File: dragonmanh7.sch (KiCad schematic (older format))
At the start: 109 parts, among them J1 USB_B, J10 Conn_02x12_Odd_Even, J11 Conn_02x03_Odd_Even, J12 VBAT+, J13 Conn_02x05_Odd_Even, J14 VBATG, J15 Conn_02x02_Odd_Even, J18 Conn_02x05_Odd_Even, J2 USB_A, J3 RJ45_Amphenol_RJMG1BD3B8K1ANR, J4 Micro_SD_Card, J5 Screw_Terminal_01x06, J6 Conn_02x12_Odd_Even, J7 USB_B, J8 Screw_Terminal_01x02, J9 Conn_02x12_Odd_Even, SW1 RESET, SW2 PC13, U1 STM32H743VITx, U10 USBLC6-2SC6, U11 SN6505, U12 TCAN332, U13 ISL83483, U14 MIC2005A, U2 KSZ8081RNA, U3 ISO1050DUB, U4 ISO3082DW, U5 S25FL127SABMFI101, U6 AP63203, U7 USBLC6-2SC6, U8 STM32F042F6Px, U9 USBLC6-2SC6, Y1 8MHz, Y2 32.768KHz, Y3 25MHz

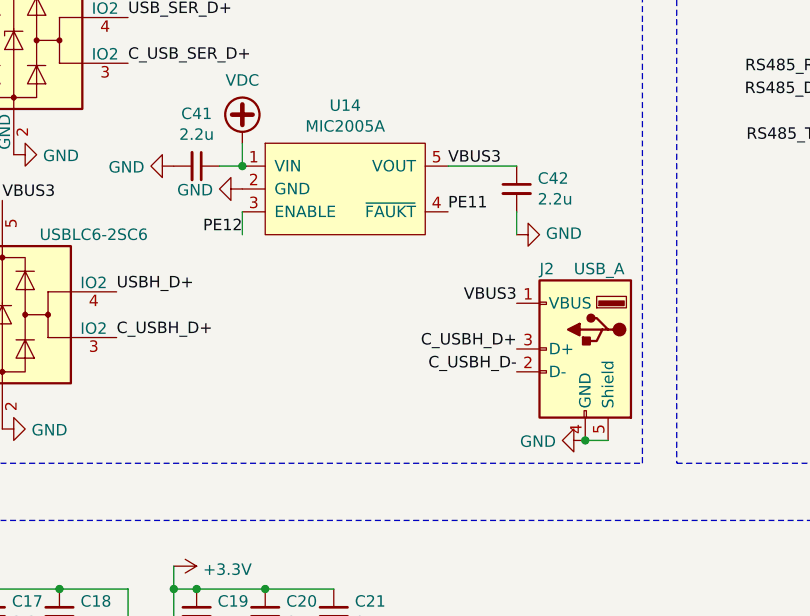
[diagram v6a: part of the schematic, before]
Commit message: Change USB connectors to more hardness versions:
 - OTG1 to USB-B
 - DAP to USB-B
 - OTG2 to USB-A horizontal rigth angle
 - Move leds and buttons to bottom side
 - Align up and bottom headers
 - Add HOST power control on OTG2

Signed-off-by: Martin Ribelotta <martinribelotta@gmail.com>
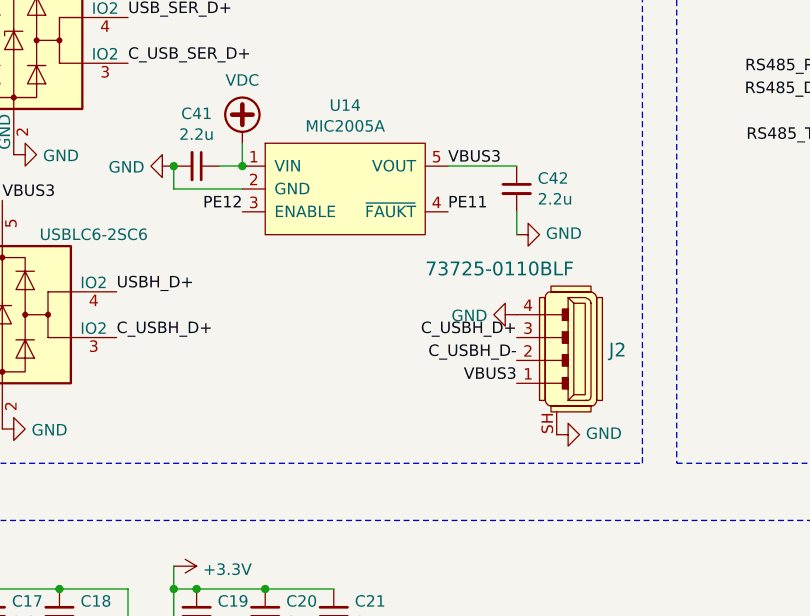
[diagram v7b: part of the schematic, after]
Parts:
- removed J2: USB_A, footprints:USB_A_Female_Vertical_RA_73725-0110BLF, symbol Connector:USB_A
- added J2: 73725-0110BLF, footprints:USB_A_Female_Vertical_RA_73725-0110BLF, symbol dk_USB-DVI-HDMI-Connectors:73725-0110BLF
- J1, J7: manf# (none) -> USB-B-S-RA-WT-SPCC
- U14: manf# (none) -> MIC2005A-2YM5-TR
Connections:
- net C_USBH_D+: now also J2.3
- net C_USBH_D-: now also J2.2
- net GND: now also J2.4, J2.SH
- net VBUS3: now also J2.1
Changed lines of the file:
@@
 C_USBD_D+
 $Comp
-L power:GND #PWR0113
-U 1 1 5C5D013E
-P 8700 7250
-F 0 "#PWR0113" H 8700 7000 50  0001 C CNN
-F 1 "GND" V 8705 7122 50  0000 R CNN
-F 2 "" H 8700 7250 50  0001 C CNN
-F 3 "" H 8700 7250 50  0001 C CNN
-	1    8700 7250
-	0    1    1    0
-$EndComp
-$Comp
 L power:GND #PWR0114
 U 1 1 5C5D01D3
@@
 	0    -1   -1   0
 $EndComp
-Text Label 10700 4200 0    50   ~ 0
-CAN_H
-Text Label 10700 4400 0    50   ~ 0
-CAN_L
-$Comp
-L power:GND #PWR0174
-U 1 1 5C7EED00
-P 10200 4700
-F 0 "#PWR0174" H 10200 4450 50  0001 C CNN
-F 1 "GND" V 10205 4572 50  0000 R CNN
-F 2 "" H 10200 4700 50  0001 C CNN
-F 3 "" H 10200 4700 50  0001 C CNN
-	1    10200 4700
-	0    -1   -1   0
-$EndComp
-Text Label 9700 4200 2    50   ~ 0
-CAN_RX
-Text Label 9700 4100 2    50   ~ 0
-CAN_TX
 $Comp
 L MCU_ST_STM32F0:STM32F042F4Px U8
@@
 Wire Wire Line
 	12050 8600 12150 8600
-Text Label 8400 6850 2    50   ~ 0
+Text Label 8400 6800 2    50   ~ 0
 C_USBH_D+
-Text Label 8400 6950 2    50   ~ 0
+Text Label 8400 6900 2    50   ~ 0
 C_USBH_D-
 $Comp
@@
 F 2 "Connector_USB:USB_B_OST_USB-B1HSxx_Horizontal" H 8850 3750 50  0001 C CNN
 F 3 " ~" H 8850 3750 50  0001 C CNN
+F 4 "USB-B-S-RA-WT-SPCC" H 8700 3800 50  0001 C CNN "manf#"
 	1    8700 3800
 	-1   0    0    -1
@@
 F 2 "Connector_USB:USB_B_OST_USB-B1HSxx_Horizontal" H 8850 4650 50  0001 C CNN
 F 3 " ~" H 8850 4650 50  0001 C CNN
+F 4 "USB-B-S-RA-WT-SPCC" H 8700 4700 50  0001 C CNN "manf#"
 	1    8700 4700
 	-1   0    0    -1
@@
 	8700 5100 8800 5100
 Connection ~ 8700 5100
-$Comp
-L Connector:USB_A J2
-U 1 1 5D52EE8F
-P 8700 6850
-F 0 "J2" H 8900 7200 50  0000 R CNN
-F 1 "USB_A" H 8750 7200 50  0000 R CNN
-F 2 "footprints:USB_A_Female_Vertical_RA_73725-0110BLF" H 8850 6800 50  0001 C CNN
-F 3 " ~" H 8850 6800 50  0001 C CNN
-	1    8700 6850
-	-1   0    0    -1
-$EndComp
-Wire Wire Line
-	8700 7250 8800 7250
-Connection ~ 8700 7250
 Wire Wire Line
 	12050 8200 12050 8600
@@
 F 2 "Package_TO_SOT_SMD:SOT-23-5" H 7650 6150 50  0001 C CNN
 F 3 "" H 7650 6150 50  0001 C CNN
+F 4 "MIC2005A-2YM5-TR" H 7650 6150 50  0001 C CNN "manf#"
 	1    7650 6150
 	1    0    0    -1
@@
 Text Label 6150 6200 0    50   ~ 0
 VBUS3
-Text Label 8400 6650 2    50   ~ 0
+Text Label 8400 7000 2    50   ~ 0
 VBUS3
 Text Label 8100 6050 0    50   ~ 0
 VBUS3
-$Comp
-L power:GND #PWR012
-U 1 1 5D4563D0
-P 7200 6150
-F 0 "#PWR012" H 7200 5900 50  0001 C CNN
-F 1 "GND" V 7205 6022 50  0000 R CNN
-F 2 "" H 7200 6150 50  0001 C CNN
-F 3 "" H 7200 6150 50  0001 C CNN
-	1    7200 6150
-	0    1    1    0
-$EndComp
 Text Label 8100 6250 0    50   ~ 0
 PE11
-Text Label 7200 6350 2    50   ~ 0
+Text Label 7200 6250 2    50   ~ 0
 PE12
-Wire Wire Line
-	7200 6350 7200 6250
 $Comp
 L Device:C_Small C42
@@
 	0    1    1    0
 $EndComp
+Text Label 9700 4100 2    50   ~ 0
+CAN_TX
+Text Label 9700 4200 2    50   ~ 0
+CAN_RX
+Text Label 10700 4200 0    50   ~ 0
+CAN_H
+Text Label 10700 4400 0    50   ~ 0
+CAN_L
+$Comp
+L power:GND #PWR0174
+U 1 1 5C7EED00
+P 10200 4700
+F 0 "#PWR0174" H 10200 4450 50  0001 C CNN
+F 1 "GND" V 10205 4572 50  0000 R CNN
+F 2 "" H 10200 4700 50  0001 C CNN
+F 3 "" H 10200 4700 50  0001 C CNN
+	1    10200 4700
+	0    -1   -1   0
+$EndComp
 $Comp
 L Interface_CAN_LIN:TCAN332 U12
@@
 	1    0    0    -1
 $EndComp
+$Comp
+L dk_USB-DVI-HDMI-Connectors:73725-0110BLF J2
+U 1 1 5D19B1BA
+P 8700 6900
+F 0 "J2" H 8597 6945 60  0000 R CNN
+F 1 "73725-0110BLF" H 9400 7300 60  0000 R CNN
+F 2 "footprints:USB_A_Female_Vertical_RA_73725-0110BLF" H 8900 7100 60  0001 L CNN
+F 3 "" H 8900 7200 60  0001 L CNN
+F 4 "609-1041-ND" H 8900 7300 60  0001 L CNN "Digi-Key_PN"
+F 5 "73725-0110BLF" H 8900 7400 60  0001 L CNN "MPN"
+F 6 "Connectors, Interconnects" H 8900 7500 60  0001 L CNN "Category"
+F 7 "USB, DVI, HDMI Connectors" H 8900 7600 60  0001 L CNN "Family"
+F 8 "http://www.amphenol-icc.com/media/wysiwyg/files/drawing/73725.pdf" H 8900 7700 60  0001 L CNN "DK_Datasheet_Link"
+F 9 "/product-detail/en/amphenol-icc-fci/73725-0110BLF/609-1041-ND/1001355" H 8900 7800 60  0001 L CNN "DK_Detail_Page"
+F 10 "CONN RCPT USB2.0 TYPEA 4POS R/A" H 8900 7900 60  0001 L CNN "Description"
+F 11 "Amphenol ICC (FCI)" H 8900 8000 60  0001 L CNN "Manufacturer"
+F 12 "Active" H 8900 8100 60  0001 L CNN "Status"
+F 13 "73725-0110BLF" H 8700 6900 50  0001 C CNN "manf#"
+	1    8700 6900
+	-1   0    0    -1
+$EndComp
+$Comp
+L power:GND #PWR0113
+U 1 1 5C5D013E
+P 8400 6700
+F 0 "#PWR0113" H 8400 6450 50  0001 C CNN
+F 1 "GND" V 8405 6572 50  0000 R CNN
+F 2 "" H 8400 6700 50  0001 C CNN
+F 3 "" H 8400 6700 50  0001 C CNN
+	1    8400 6700
+	0    1    1    0
+$EndComp
+$Comp
+L power:GND #PWR0186
+U 1 1 5D1CC21D
+P 8575 7225
+F 0 "#PWR0186" H 8575 6975 50  0001 C CNN
+F 1 "GND" V 8580 7097 50  0000 R CNN
+F 2 "" H 8575 7225 50  0001 C CNN
+F 3 "" H 8575 7225 50  0001 C CNN
+	1    8575 7225
+	0    -1   -1   0
+$EndComp
+Wire Wire Line
+	7200 6150 6900 6150
+Wire Wire Line
+	6900 6150 6900 6050
+Connection ~ 6900 6050
 $EndSCHEMATC

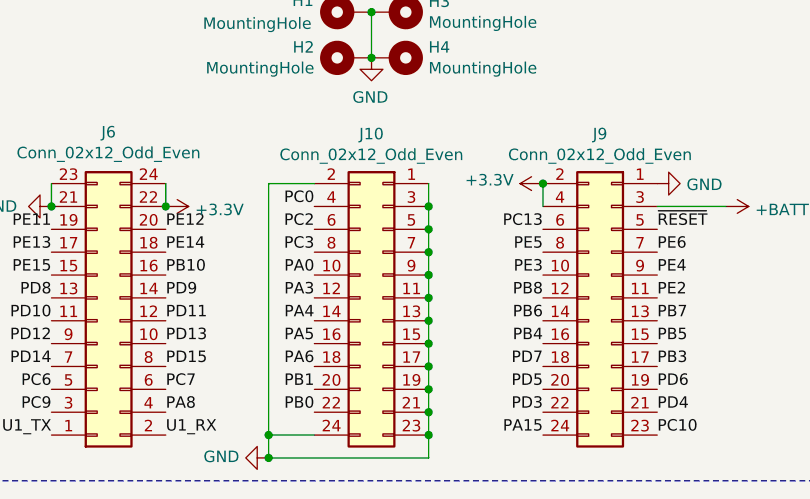
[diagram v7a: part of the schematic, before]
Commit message: Fix gnd plane beside RJ45
Signed-off-by: Martin Ribelotta <martinribelotta@gmail.com>
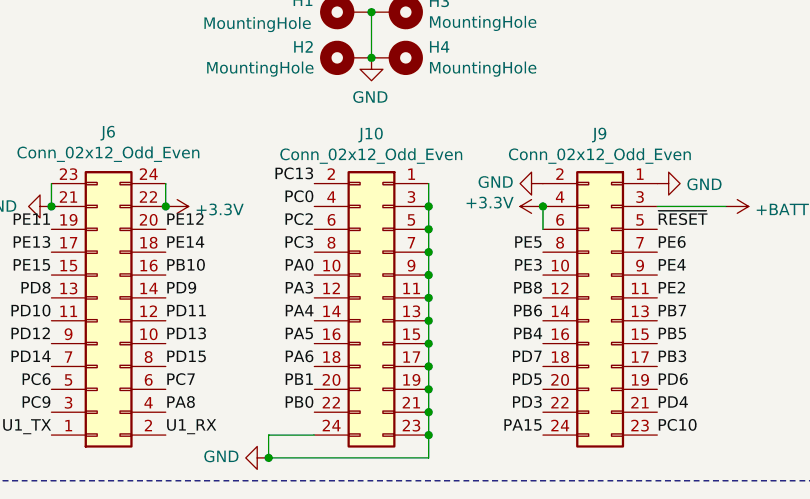
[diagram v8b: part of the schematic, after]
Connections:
- net +3V3: now also J9.6 (Pin_6); no longer J9.2 (Pin_2)
- net GND: now also J9.2 (Pin_2); no longer J10.2 (Pin_2)
- net PC13: now also J10.2 (Pin_2); no longer J9.6 (Pin_6)
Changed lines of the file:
@@
 Text Label 3800 9800 0    50   ~ 0
 PE6
-Text Label 3300 9700 2    50   ~ 0
+Text Label 2300 9500 2    50   ~ 0
 PC13
 $Comp
 L power:+3.3V #PWR0153
 U 1 1 5C7A85C0
-P 3300 9500
-F 0 "#PWR0153" H 3300 9350 50  0001 C CNN
-F 1 "+3.3V" V 3315 9628 50  0000 L CNN
-F 2 "" H 3300 9500 50  0001 C CNN
-F 3 "" H 3300 9500 50  0001 C CNN
-	1    3300 9500
-	0    -1   -1   0
-$EndComp
-Wire Wire Line
-	3300 9600 3300 9500
+P 3300 9600
+F 0 "#PWR0153" H 3300 9450 50  0001 C CNN
+F 1 "+3.3V" V 3315 9728 50  0000 L CNN
+F 2 "" H 3300 9600 50  0001 C CNN
+F 3 "" H 3300 9600 50  0001 C CNN
+	1    3300 9600
+	0    -1   -1   0
+$EndComp
 $Comp
 L power:GND #PWR0154
@@
 	2100 10700 2800 10700
 Wire Wire Line
-	2100 9500 2100 10600
-Connection ~ 2100 10600
-Wire Wire Line
 	2100 10600 2100 10700
 $Comp
@@
 Wire Wire Line
 	2300 10600 2100 10600
-Wire Wire Line
-	2300 9500 2100 9500
 $Comp
 L Connector_Generic:Conn_02x12_Odd_Even J10
@@
 Wire Wire Line
 	2100 1350 2400 1350
-Connection ~ 3300 9500
 $Comp
 L Connector_Generic:Conn_02x12_Odd_Even J9
@@
 	6900 6150 6900 6050
 Connection ~ 6900 6050
+Wire Wire Line
+	3300 9700 3300 9600
+Connection ~ 3300 9600
+$Comp
+L power:GND #PWR?
+U 1 1 5D193CC5
+P 3300 9500
+F 0 "#PWR?" H 3300 9250 50  0001 C CNN
+F 1 "GND" V 3305 9372 50  0000 R CNN
+F 2 "" H 3300 9500 50  0001 C CNN
+F 3 "" H 3300 9500 50  0001 C CNN
+	1    3300 9500
+	0    1    -1   0
+$EndComp
 $EndSCHEMATC
